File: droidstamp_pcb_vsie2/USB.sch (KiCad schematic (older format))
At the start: 35 parts, among them J3 USB_2A, U4 GL850G, U5 RCLAMP0502B, U6 RCLAMP0502B, U7 RCLAMP0502B, U8 RCLAMP0502B, X2 12MHz

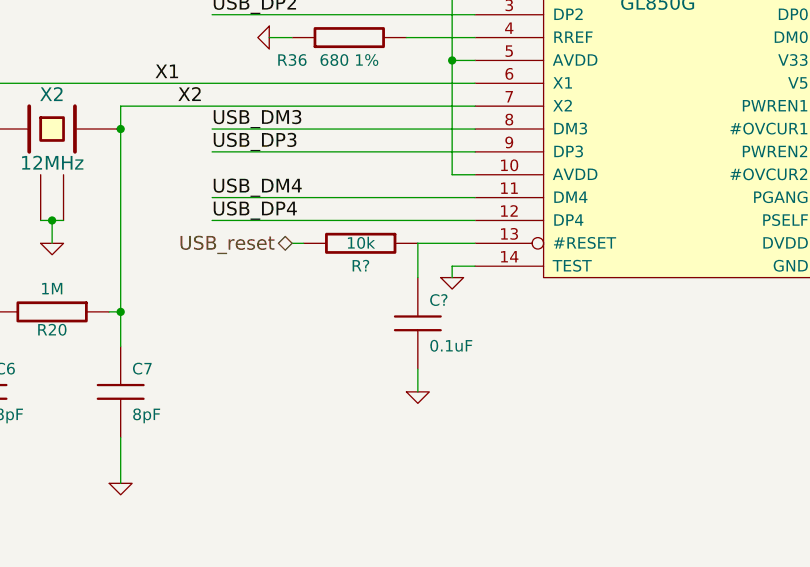
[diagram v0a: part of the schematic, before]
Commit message: se inserto el smt32f4
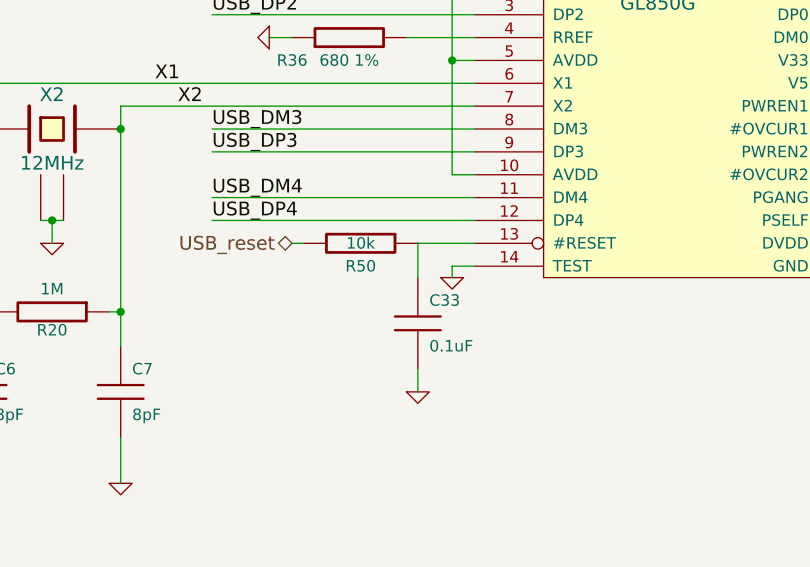
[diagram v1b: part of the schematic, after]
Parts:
- gave numbers to parts that had none: 2
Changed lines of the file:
@@
-EESchema Schematic File Version 2  date sáb 03 mar 2012 09:20:54 COT
+EESchema Schematic File Version 2  date Thu 29 Mar 2012 07:34:40 PM COT
 LIBS:con-jack
 LIBS:adm3101e
@@
 LIBS:lt1117cst
 LIBS:zxmhc3f381n8
+LIBS:stm32f4_lqfp100
 LIBS:i.mx233stamp-cache
-EELAYER 24  0
+EELAYER 25  0
 EELAYER END
-$Descr A4 11700 8267
+$Descr A4 11693 8268
+encoding utf-8
 Sheet 5 5
 Title ""
-Date "3 mar 2012"
+Date "30 mar 2012"
 Rev ""
 Comp ""
@@
 	6550 3200 6800 3200
 $Comp
-L C C?
+L C C33
 U 1 1 4F522649
 P 6550 3550
-F 0 "C?" H 6600 3650 50  0000 L CNN
+F 0 "C33" H 6600 3650 50  0000 L CNN
 F 1 "0.1uF" H 6600 3450 50  0000 L CNN
 F 2 "SM0603" H 6550 3550 60  0001 C CNN
@@
 $EndComp
 $Comp
-L GND #PWR?
+L GND #PWR133
 U 1 1 4F522478
 P 6550 3850
-F 0 "#PWR?" H 6550 3850 30  0001 C CNN
+F 0 "#PWR133" H 6550 3850 30  0001 C CNN
 F 1 "GND" H 6550 3780 30  0001 C CNN
 	1    6550 3850
@@
 $EndComp
 $Comp
-L R R?
+L R R50
 U 1 1 4F522458
 P 6300 3200
-F 0 "R?" V 6400 3200 50  0000 C CNN
+F 0 "R50" V 6400 3200 50  0000 C CNN
 F 1 "10k" V 6300 3200 50  0000 C CNN
 F 2 "SM0603" H 6300 3200 60  0001 C CNN
@@
 USM_P2
 $Comp
-L VDDIO_3V3 #PWR0112
+L VDDIO_3V3 #PWR132
 U 1 1 4E5BAA82
 P 6500 1750
-F 0 "#PWR0112" H 6500 1850 30  0001 C CNN
+F 0 "#PWR132" H 6500 1850 30  0001 C CNN
 F 1 "VDDIO_3V3" H 6500 1850 30  0000 C CNN
 	1    6500 1750
@@
 $EndComp
 $Comp
-L GND #PWR0113
+L GND #PWR129
 U 1 1 4E43139E
 P 4950 3200
-F 0 "#PWR0113" H 4950 3200 30  0001 C CNN
+F 0 "#PWR129" H 4950 3200 30  0001 C CNN
 F 1 "GND" H 4950 3130 30  0001 C CNN
 	1    4950 3200
@@
 $EndComp
 $Comp
-L GND #PWR0114
+L GND #PWR134
 U 1 1 4E41C8A5
 P 6700 3350
-F 0 "#PWR0114" H 6700 3350 30  0001 C CNN
+F 0 "#PWR134" H 6700 3350 30  0001 C CNN
 F 1 "GND" H 6700 3280 30  0001 C CNN
 	1    6700 3350
@@
 $EndComp
 $Comp
-L GND #PWR0116
+L GND #PWR125
 U 1 1 4E4157F8
 P 3950 4850
-F 0 "#PWR0116" H 3950 4850 30  0001 C CNN
+F 0 "#PWR125" H 3950 4850 30  0001 C CNN
 F 1 "GND" H 3950 4780 30  0001 C CNN
 	1    3950 4850
@@
 $EndComp
 $Comp
-L GND #PWR0117
+L GND #PWR124
 U 1 1 4E4157E9
 P 3950 3800
-F 0 "#PWR0117" H 3950 3800 30  0001 C CNN
+F 0 "#PWR124" H 3950 3800 30  0001 C CNN
 F 1 "GND" H 3950 3730 30  0001 C CNN
 	1    3950 3800
@@
 $EndComp
 $Comp
-L GND #PWR0118
+L GND #PWR127
 U 1 1 4E4157C0
 P 4000 2650
-F 0 "#PWR0118" H 4000 2650 30  0001 C CNN
+F 0 "#PWR127" H 4000 2650 30  0001 C CNN
 F 1 "GND" H 4000 2580 30  0001 C CNN
 	1    4000 2650
@@
 $EndComp
 $Comp
-L GND #PWR0119
+L GND #PWR126
 U 1 1 4E4157B3
 P 4000 1350
-F 0 "#PWR0119" H 4000 1350 30  0001 C CNN
+F 0 "#PWR126" H 4000 1350 30  0001 C CNN
 F 1 "GND" H 4000 1280 30  0001 C CNN
 	1    4000 1350
@@
 $EndComp
 $Comp
-L GND #PWR0120
+L GND #PWR122
 U 1 1 4E415157
 P 1100 2050
-F 0 "#PWR0120" H 1100 2050 30  0001 C CNN
+F 0 "#PWR122" H 1100 2050 30  0001 C CNN
 F 1 "GND" H 1100 1980 30  0001 C CNN
 	1    1100 2050
@@
 $EndComp
 $Comp
-L GND #PWR0121
+L GND #PWR123
 U 1 1 4E414F30
 P 2400 2100
-F 0 "#PWR0121" H 2400 2100 30  0001 C CNN
+F 0 "#PWR123" H 2400 2100 30  0001 C CNN
 F 1 "GND" H 2400 2030 30  0001 C CNN
 	1    2400 2100
@@
 $EndComp
 $Comp
-L VDD5V #PWR0122
+L VDD5V #PWR121
 U 1 1 4E414E3D
 P 650 1150
-F 0 "#PWR0122" H 650 1250 30  0001 C CNN
+F 0 "#PWR121" H 650 1250 30  0001 C CNN
 F 1 "VDD5V" H 650 1250 30  0000 C CNN
 	1    650  1150
@@
 $EndComp
 $Comp
-L GND #PWR0123
+L GND #PWR136
 U 1 1 4E3C4430
 P 7400 1400
-F 0 "#PWR0123" H 7400 1400 30  0001 C CNN
+F 0 "#PWR136" H 7400 1400 30  0001 C CNN
 F 1 "GND" H 7400 1330 30  0001 C CNN
 	1    7400 1400
@@
 $EndComp
 $Comp
-L VDD5V #PWR0124
+L VDD5V #PWR135
 U 1 1 4E3C4429
 P 7400 800
-F 0 "#PWR0124" H 7400 900 30  0001 C CNN
+F 0 "#PWR135" H 7400 900 30  0001 C CNN
 F 1 "VDD5V" H 7400 900 30  0000 C CNN
 	1    7400 800
@@
 $EndComp
 $Comp
-L VDD5V #PWR0125
+L VDD5V #PWR140
 U 1 1 4E3C4418
 P 9000 2500
-F 0 "#PWR0125" H 9000 2600 30  0001 C CNN
+F 0 "#PWR140" H 9000 2600 30  0001 C CNN
 F 1 "VDD5V" H 9000 2600 30  0000 C CNN
 	1    9000 2500
@@
 $EndComp
 $Comp
-L GND #PWR0126
+L GND #PWR138
 U 1 1 4E3C436B
 P 7900 1600
-F 0 "#PWR0126" H 7900 1600 30  0001 C CNN
+F 0 "#PWR138" H 7900 1600 30  0001 C CNN
 F 1 "GND" H 7900 1530 30  0001 C CNN
 	1    7900 1600
@@
 USBH_P33V
 $Comp
-L VDD5V #PWR0127
+L VDD5V #PWR141
 U 1 1 4E3C4207
 P 9000 2900
-F 0 "#PWR0127" H 9000 3000 30  0001 C CNN
+F 0 "#PWR141" H 9000 3000 30  0001 C CNN
 F 1 "VDD5V" H 9000 3000 30  0000 C CNN
 	1    9000 2900
@@
 USBH_P33V
 $Comp
-L GND #PWR0128
+L GND #PWR142
 U 1 1 4E3C3A60
 P 9300 5550
-F 0 "#PWR0128" H 9300 5550 30  0001 C CNN
+F 0 "#PWR142" H 9300 5550 30  0001 C CNN
 F 1 "GND" H 9300 5480 30  0001 C CNN
 	1    9300 5550
@@
 $EndComp
 $Comp
-L GND #PWR0129
+L GND #PWR137
 U 1 1 4E3C3A56
 P 7400 5550
-F 0 "#PWR0129" H 7400 5550 30  0001 C CNN
+F 0 "#PWR137" H 7400 5550 30  0001 C CNN
 F 1 "GND" H 7400 5480 30  0001 C CNN
 	1    7400 5550
@@
 andres.calderon@emqbit.com\n
 $Comp
-L GND #PWR0130
+L GND #PWR131
 U 1 1 4E3C3807
 P 5900 2300
-F 0 "#PWR0130" H 5900 2300 30  0001 C CNN
+F 0 "#PWR131" H 5900 2300 30  0001 C CNN
 F 1 "GND" H 5900 2230 30  0001 C CNN
 	1    5900 2300
@@
 $EndComp
 $Comp
-L GND #PWR0131
+L GND #PWR143
 U 1 1 4E3C36BE
 P 9800 3550
-F 0 "#PWR0131" H 9800 3550 30  0001 C CNN
+F 0 "#PWR143" H 9800 3550 30  0001 C CNN
 F 1 "GND" H 9800 3480 30  0001 C CNN
 	1    9800 3550
@@
 X1
 $Comp
-L GND #PWR0132
+L GND #PWR139
 U 1 1 4E3C222B
 P 8900 3700
-F 0 "#PWR0132" H 8900 3700 30  0001 C CNN
+F 0 "#PWR139" H 8900 3700 30  0001 C CNN
 F 1 "GND" H 8900 3630 30  0001 C CNN
 	1    8900 3700
@@
 USB_DM2
 $Comp
-L GND #PWR0133
+L GND #PWR128
 U 1 1 4E3C212B
 P 4650 4250
-F 0 "#PWR0133" H 4650 4250 30  0001 C CNN
+F 0 "#PWR128" H 4650 4250 30  0001 C CNN
 F 1 "GND" H 4650 4180 30  0001 C CNN
 	1    4650 4250
@@
 $EndComp
 $Comp
-L GND #PWR0134
+L GND #PWR130
 U 1 1 4E3C206C
 P 5250 4250
-F 0 "#PWR0134" H 5250 4250 30  0001 C CNN
+F 0 "#PWR130" H 5250 4250 30  0001 C CNN
 F 1 "GND" H 5250 4180 30  0001 C CNN
 	1    5250 4250

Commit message: sync with las sie_bot_v2
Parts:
- renumbered C33 to C77
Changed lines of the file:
@@
-EESchema Schematic File Version 2  date Thu 29 Mar 2012 07:34:40 PM COT
+EESchema Schematic File Version 2  date Fri 30 Mar 2012 08:38:46 AM COT
 LIBS:con-jack
 LIBS:adm3101e
@@
 LIBS:lt1117cst
 LIBS:zxmhc3f381n8
-LIBS:stm32f4_lqfp100
 LIBS:i.mx233stamp-cache
 EELAYER 25  0
 EELAYER END
-$Descr A4 11693 8268
+$Descr A4 11700 8267
 encoding utf-8
 Sheet 5 5
@@
 	6550 3200 6800 3200
 $Comp
-L C C33
+L C C77
 U 1 1 4F522649
 P 6550 3550
-F 0 "C33" H 6600 3650 50  0000 L CNN
+F 0 "C77" H 6600 3650 50  0000 L CNN
 F 1 "0.1uF" H 6600 3450 50  0000 L CNN
 F 2 "SM0603" H 6550 3550 60  0001 C CNN
@@
 $EndComp
 $Comp
-L GND #PWR133
+L GND #PWR?
 U 1 1 4F522478
 P 6550 3850
-F 0 "#PWR133" H 6550 3850 30  0001 C CNN
+F 0 "#PWR?" H 6550 3850 30  0001 C CNN
 F 1 "GND" H 6550 3780 30  0001 C CNN
 	1    6550 3850
@@
 USM_P2
 $Comp
-L VDDIO_3V3 #PWR132
+L VDDIO_3V3 #PWR0112
 U 1 1 4E5BAA82
 P 6500 1750
-F 0 "#PWR132" H 6500 1850 30  0001 C CNN
+F 0 "#PWR0112" H 6500 1850 30  0001 C CNN
 F 1 "VDDIO_3V3" H 6500 1850 30  0000 C CNN
 	1    6500 1750
@@
 $EndComp
 $Comp
-L GND #PWR129
+L GND #PWR0113
 U 1 1 4E43139E
 P 4950 3200
-F 0 "#PWR129" H 4950 3200 30  0001 C CNN
+F 0 "#PWR0113" H 4950 3200 30  0001 C CNN
 F 1 "GND" H 4950 3130 30  0001 C CNN
 	1    4950 3200
@@
 $EndComp
 $Comp
-L GND #PWR134
+L GND #PWR0114
 U 1 1 4E41C8A5
 P 6700 3350
-F 0 "#PWR134" H 6700 3350 30  0001 C CNN
+F 0 "#PWR0114" H 6700 3350 30  0001 C CNN
 F 1 "GND" H 6700 3280 30  0001 C CNN
 	1    6700 3350
@@
 $EndComp
 $Comp
-L GND #PWR125
+L GND #PWR0116
 U 1 1 4E4157F8
 P 3950 4850
-F 0 "#PWR125" H 3950 4850 30  0001 C CNN
+F 0 "#PWR0116" H 3950 4850 30  0001 C CNN
 F 1 "GND" H 3950 4780 30  0001 C CNN
 	1    3950 4850
@@
 $EndComp
 $Comp
-L GND #PWR124
+L GND #PWR0117
 U 1 1 4E4157E9
 P 3950 3800
-F 0 "#PWR124" H 3950 3800 30  0001 C CNN
+F 0 "#PWR0117" H 3950 3800 30  0001 C CNN
 F 1 "GND" H 3950 3730 30  0001 C CNN
 	1    3950 3800
@@
 $EndComp
 $Comp
-L GND #PWR127
+L GND #PWR0118
 U 1 1 4E4157C0
 P 4000 2650
-F 0 "#PWR127" H 4000 2650 30  0001 C CNN
+F 0 "#PWR0118" H 4000 2650 30  0001 C CNN
 F 1 "GND" H 4000 2580 30  0001 C CNN
 	1    4000 2650
@@
 $EndComp
 $Comp
-L GND #PWR126
+L GND #PWR0119
 U 1 1 4E4157B3
 P 4000 1350
-F 0 "#PWR126" H 4000 1350 30  0001 C CNN
+F 0 "#PWR0119" H 4000 1350 30  0001 C CNN
 F 1 "GND" H 4000 1280 30  0001 C CNN
 	1    4000 1350
@@
 $EndComp
 $Comp
-L GND #PWR122
+L GND #PWR0120
 U 1 1 4E415157
 P 1100 2050
-F 0 "#PWR122" H 1100 2050 30  0001 C CNN
+F 0 "#PWR0120" H 1100 2050 30  0001 C CNN
 F 1 "GND" H 1100 1980 30  0001 C CNN
 	1    1100 2050
@@
 $EndComp
 $Comp
-L GND #PWR123
+L GND #PWR0121
 U 1 1 4E414F30
 P 2400 2100
-F 0 "#PWR123" H 2400 2100 30  0001 C CNN
+F 0 "#PWR0121" H 2400 2100 30  0001 C CNN
 F 1 "GND" H 2400 2030 30  0001 C CNN
 	1    2400 2100
@@
 $EndComp
 $Comp
-L VDD5V #PWR121
+L VDD5V #PWR0122
 U 1 1 4E414E3D
 P 650 1150
-F 0 "#PWR121" H 650 1250 30  0001 C CNN
+F 0 "#PWR0122" H 650 1250 30  0001 C CNN
 F 1 "VDD5V" H 650 1250 30  0000 C CNN
 	1    650  1150
@@
 $EndComp
 $Comp
-L GND #PWR136
+L GND #PWR0123
 U 1 1 4E3C4430
 P 7400 1400
-F 0 "#PWR136" H 7400 1400 30  0001 C CNN
+F 0 "#PWR0123" H 7400 1400 30  0001 C CNN
 F 1 "GND" H 7400 1330 30  0001 C CNN
 	1    7400 1400
@@
 $EndComp
 $Comp
-L VDD5V #PWR135
+L VDD5V #PWR0124
 U 1 1 4E3C4429
 P 7400 800
-F 0 "#PWR135" H 7400 900 30  0001 C CNN
+F 0 "#PWR0124" H 7400 900 30  0001 C CNN
 F 1 "VDD5V" H 7400 900 30  0000 C CNN
 	1    7400 800
@@
 $EndComp
 $Comp
-L VDD5V #PWR140
+L VDD5V #PWR0125
 U 1 1 4E3C4418
 P 9000 2500
-F 0 "#PWR140" H 9000 2600 30  0001 C CNN
+F 0 "#PWR0125" H 9000 2600 30  0001 C CNN
 F 1 "VDD5V" H 9000 2600 30  0000 C CNN
 	1    9000 2500
@@
 $EndComp
 $Comp
-L GND #PWR138
+L GND #PWR0126
 U 1 1 4E3C436B
 P 7900 1600
-F 0 "#PWR138" H 7900 1600 30  0001 C CNN
+F 0 "#PWR0126" H 7900 1600 30  0001 C CNN
 F 1 "GND" H 7900 1530 30  0001 C CNN
 	1    7900 1600
@@
 USBH_P33V
 $Comp
-L VDD5V #PWR141
+L VDD5V #PWR0127
 U 1 1 4E3C4207
 P 9000 2900
-F 0 "#PWR141" H 9000 3000 30  0001 C CNN
+F 0 "#PWR0127" H 9000 3000 30  0001 C CNN
 F 1 "VDD5V" H 9000 3000 30  0000 C CNN
 	1    9000 2900
@@
 USBH_P33V
 $Comp
-L GND #PWR142
+L GND #PWR0128
 U 1 1 4E3C3A60
 P 9300 5550
-F 0 "#PWR142" H 9300 5550 30  0001 C CNN
+F 0 "#PWR0128" H 9300 5550 30  0001 C CNN
 F 1 "GND" H 9300 5480 30  0001 C CNN
 	1    9300 5550
@@
 $EndComp
 $Comp
-L GND #PWR137
+L GND #PWR0129
 U 1 1 4E3C3A56
 P 7400 5550
-F 0 "#PWR137" H 7400 5550 30  0001 C CNN
+F 0 "#PWR0129" H 7400 5550 30  0001 C CNN
 F 1 "GND" H 7400 5480 30  0001 C CNN
 	1    7400 5550
@@
 andres.calderon@emqbit.com\n
 $Comp
-L GND #PWR131
+L GND #PWR0130
 U 1 1 4E3C3807
 P 5900 2300
-F 0 "#PWR131" H 5900 2300 30  0001 C CNN
+F 0 "#PWR0130" H 5900 2300 30  0001 C CNN
 F 1 "GND" H 5900 2230 30  0001 C CNN
 	1    5900 2300
@@
 $EndComp
 $Comp
-L GND #PWR143
+L GND #PWR0131
 U 1 1 4E3C36BE
 P 9800 3550
-F 0 "#PWR143" H 9800 3550 30  0001 C CNN
+F 0 "#PWR0131" H 9800 3550 30  0001 C CNN
 F 1 "GND" H 9800 3480 30  0001 C CNN
 	1    9800 3550
@@
 X1
 $Comp
-L GND #PWR139
+L GND #PWR0132
 U 1 1 4E3C222B
 P 8900 3700
-F 0 "#PWR139" H 8900 3700 30  0001 C CNN
+F 0 "#PWR0132" H 8900 3700 30  0001 C CNN
 F 1 "GND" H 8900 3630 30  0001 C CNN
 	1    8900 3700
@@
 USB_DM2
 $Comp
-L GND #PWR128
+L GND #PWR0133
 U 1 1 4E3C212B
 P 4650 4250
-F 0 "#PWR128" H 4650 4250 30  0001 C CNN
+F 0 "#PWR0133" H 4650 4250 30  0001 C CNN
 F 1 "GND" H 4650 4180 30  0001 C CNN
 	1    4650 4250
@@
 $EndComp
 $Comp
-L GND #PWR130
+L GND #PWR0134
 U 1 1 4E3C206C
 P 5250 4250
-F 0 "#PWR130" H 5250 4250 30  0001 C CNN
+F 0 "#PWR0134" H 5250 4250 30  0001 C CNN
 F 1 "GND" H 5250 4180 30  0001 C CNN
 	1    5250 4250
